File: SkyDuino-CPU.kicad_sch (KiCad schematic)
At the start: 38 parts, among them J11 DBG, J12 USB-A RMT, J13 DISP, J14 USB_C Artisan, SW1 BOOT, U10 USBLC6-2SC6, U7 25MHz, U8 USBLC6-2SC6, U9 STM32F411RET6, Y1 32.768kHz

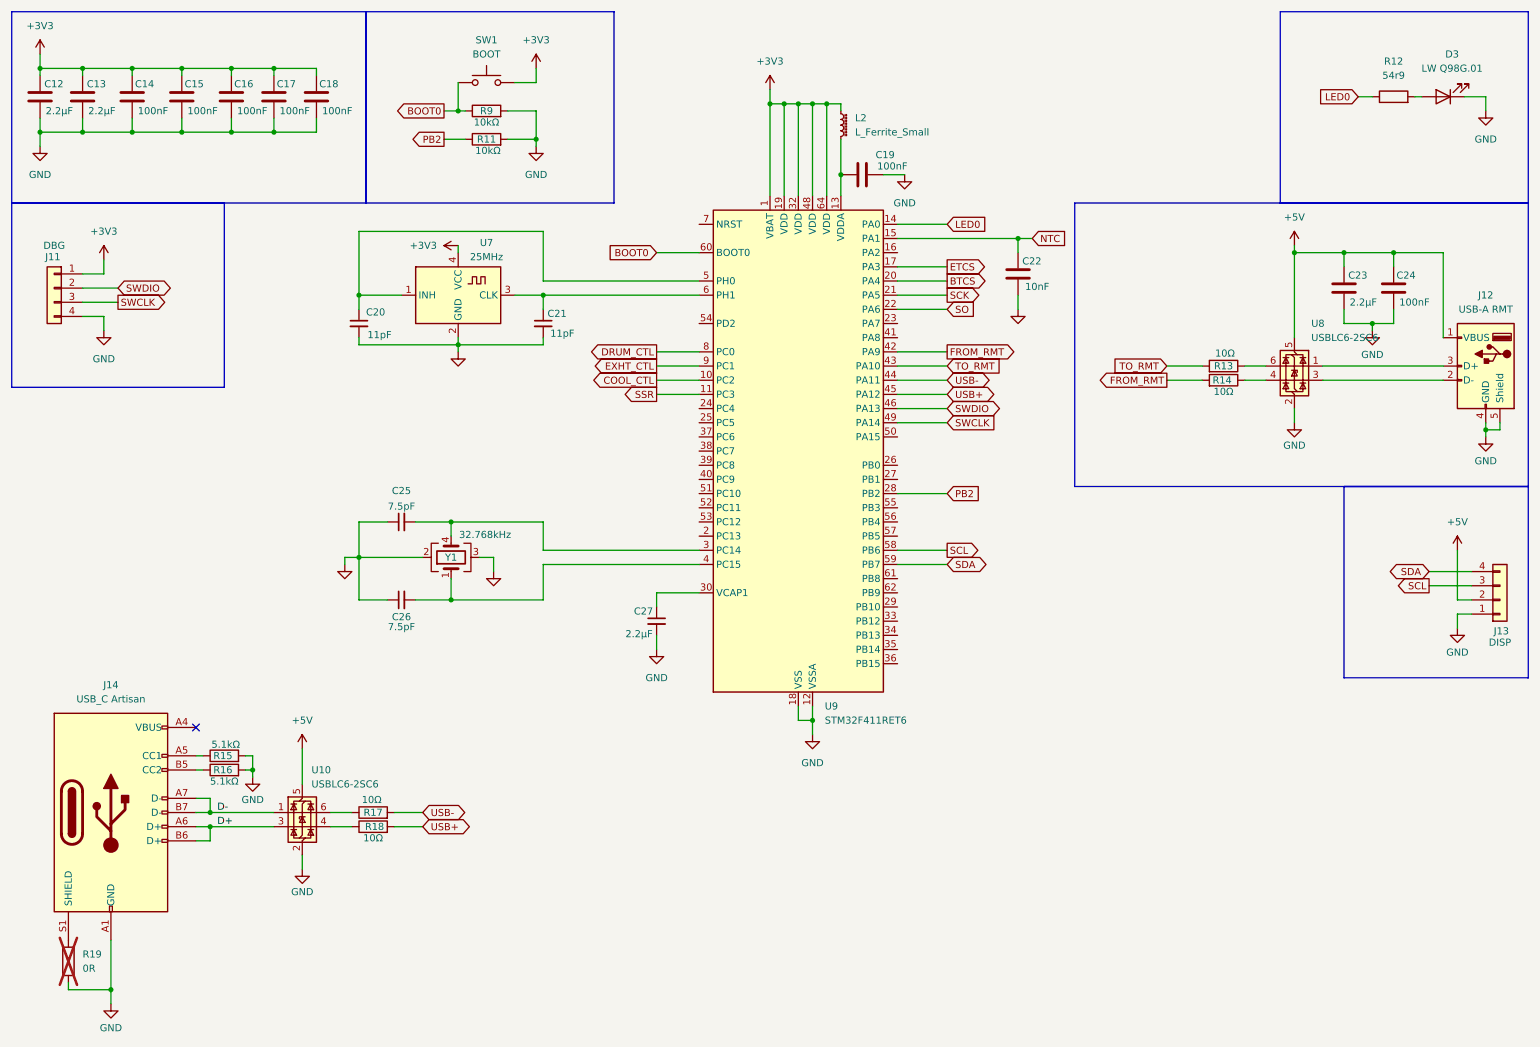
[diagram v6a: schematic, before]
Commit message: Use ferrite bead for AVDD
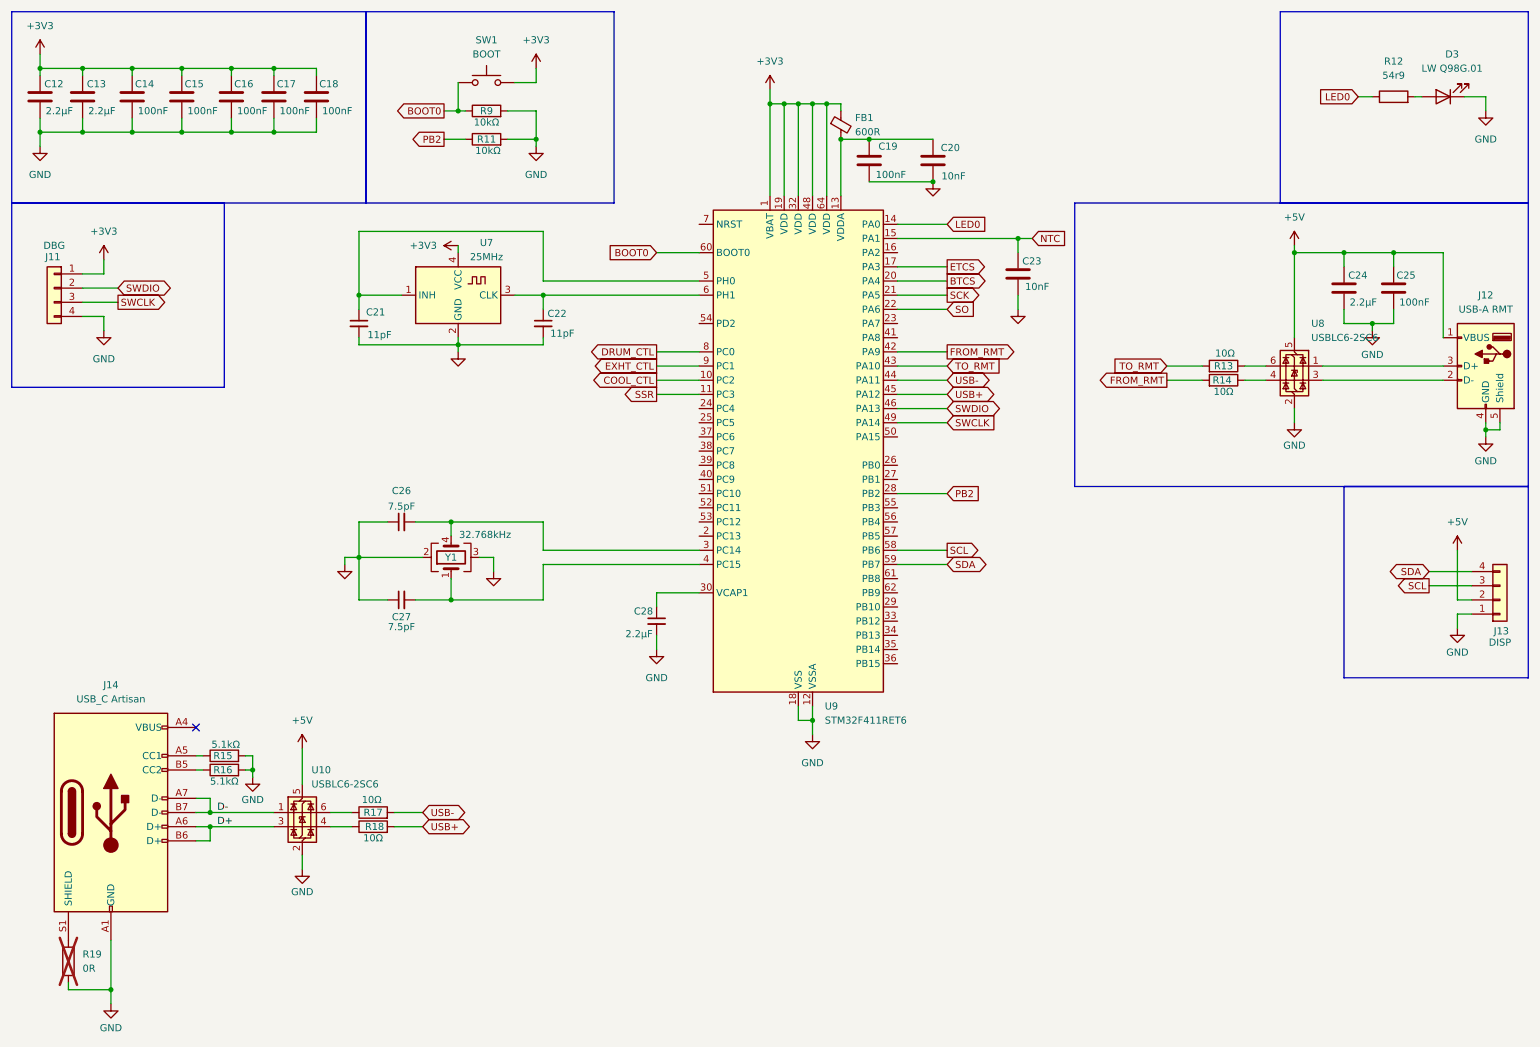
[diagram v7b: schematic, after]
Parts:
- removed L2: L_Ferrite_Small, symbol Device:L_Ferrite_Small
- added C20: 10nF, Capacitor_SMD:C_0805_2012Metric_Pad1.18x1.45mm_HandSolder, symbol Device:C
- added FB1: 600R, Inductor_SMD:L_0805_2012Metric_Pad1.05x1.20mm_HandSolder, symbol Device:FerriteBead_Small
- renumbered C20 to C21, C21 to C22, C22 to C23, C23 to C24, C24 to C25, C25 to C26, C26 to C27, C27 to C28
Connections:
- net +3V3: now also FB1.1
- net GND: now also C19.1, C20.1; no longer C19.2
- net at U9.13 (VDDA): now also C19.2, C20.2, FB1.2; no longer C19.1
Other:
- moved on the sheet: C19

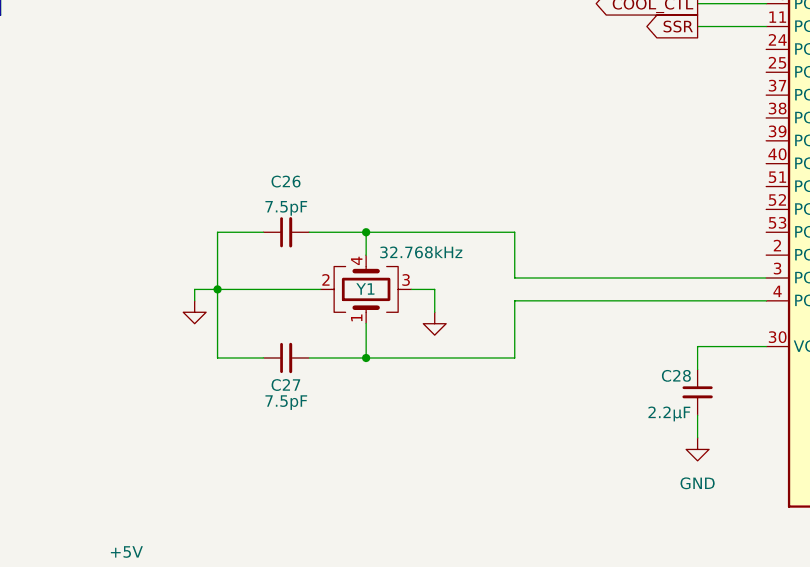
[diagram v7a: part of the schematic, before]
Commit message: Optimize pinouts
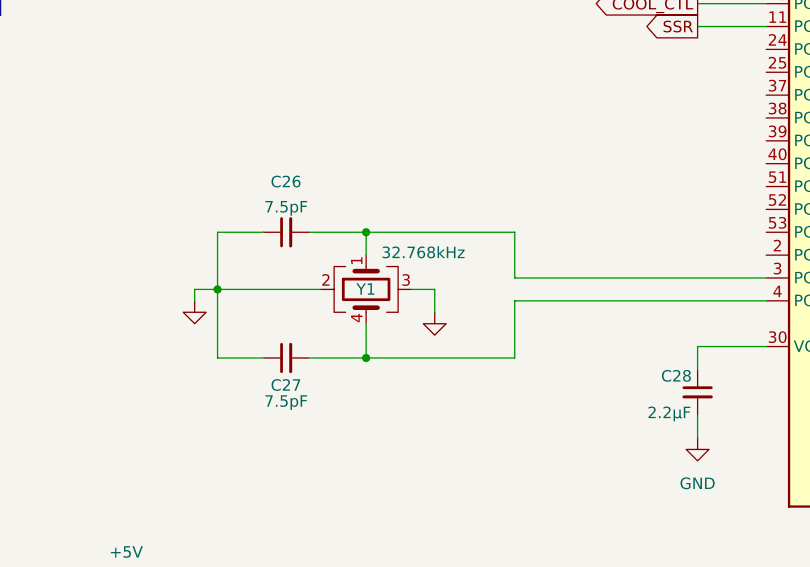
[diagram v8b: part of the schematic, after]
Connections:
- net at C26.2, U9.3 (PC14): now also Y1.1; no longer Y1.4
- net at C27.2, U9.4 (PC15): now also Y1.4; no longer Y1.1
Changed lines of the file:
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@@
 		(lib_id "Device:Crystal_GND23")
 		(at 91.44 111.76 90)
+		(mirror x)
 		(unit 1)
 		(exclude_from_sim no)
@@
 		)
 		(property "Value" "32.768kHz"
-			(at 97.536 107.696 90)
+			(at 97.79 107.696 90)
 			(effects
 				(font
